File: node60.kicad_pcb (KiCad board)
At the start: 2 copper layers, 0 parts

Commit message: DEC-020: flipped 2.6 mm board, enclosure connector placement, 3D mockup
The board mounts component side down under the lid and is 2.6 mm thick,
so the SurLok Plus receptacles in the lid reach the REDCUBE 74660016R
terminals through the board (user's decisions, 2026-10-30).

- PCB: J901-J912 placed and locked, 250 x 160 mm provisional outline,
  2.6 mm thickness. Outputs on a 40 mm pitch; KiCad view mirrored
  against the outside view (scripts/place_connectors.py).
- Lid terminals on a symmetric grid: battery +-48 mm, return +-75 mm.
  scripts/check_surlok_clearance.py checks all 81 west/north/east plug
  combinations and keeps east/west plugs inside the walls.
- Architecture site: DEC-020, harness page section, Rev B entry, and the
  3D enclosure mockup served at /mockups/ (wrapped by the docs build).

Open: AT13/ATM13 pin tails protrude only 0.1-0.5 mm on 2.6 mm. CI now
runs DRC with schematic parity, which fails until layout is complete.

Co-Authored-By: Claude Opus 5.5 <noreply@anthropic.com>
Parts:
- added J901: 74660016R, DropOut_TerminalBlock_Wuerth:Wuerth_REDCUBE-SMT_WP-SMRT_74660016, F.Cu at (107.0, 125.0)
- added J902: 74660016R, DropOut_TerminalBlock_Wuerth:Wuerth_REDCUBE-SMT_WP-SMRT_74660016, F.Cu at (80.0, 65.0)
- added J903: ATM13-2P-BM04, DropOut_Connector_Amphenol:Amphenol_ATM13-2P-BMxx_1x02_P4.20mm_Horizontal, F.Cu at (46.0, 91.9)
- added J904: AT13-2P-BM04, DropOut_Connector_Amphenol:Amphenol_AT13-2P-BMxx_1x02_P5.40mm_Horizontal, F.Cu at (252.3, 175.0)
- added J905: AT13-2P-BM04, DropOut_Connector_Amphenol:Amphenol_AT13-2P-BMxx_1x02_P5.40mm_Horizontal, F.Cu at (212.3, 175.0)
- added J906: AT13-2P-BM04, DropOut_Connector_Amphenol:Amphenol_AT13-2P-BMxx_1x02_P5.40mm_Horizontal, F.Cu at (172.3, 175.0)
- added J907: AT13-2P-BM04, DropOut_Connector_Amphenol:Amphenol_AT13-2P-BMxx_1x02_P5.40mm_Horizontal, F.Cu at (132.3, 175.0)
- added J908: AT13-2P-BM04, DropOut_Connector_Amphenol:Amphenol_AT13-2P-BMxx_1x02_P5.40mm_Horizontal, F.Cu at (92.3, 175.0)
- added J909: AT13-2P-BM04, DropOut_Connector_Amphenol:Amphenol_AT13-2P-BMxx_1x02_P5.40mm_Horizontal, F.Cu at (52.3, 175.0)
- added J910: 74660016R, DropOut_TerminalBlock_Wuerth:Wuerth_REDCUBE-SMT_WP-SMRT_74660016, F.Cu at (203.0, 125.0)
- added J911: 74660016R, DropOut_TerminalBlock_Wuerth:Wuerth_REDCUBE-SMT_WP-SMRT_74660016, F.Cu at (230.0, 65.0)
- added J912: ATM13-2P-BM04, DropOut_Connector_Amphenol:Amphenol_ATM13-2P-BMxx_1x02_P4.20mm_Horizontal, F.Cu at (264.0, 96.1)
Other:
- board outline added: 250 x 160 mm

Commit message: DEC-021: board component side up, busbars, raised-T lid, T1S on north wall
The user changed the mechanical design on 2026-10-30 and accepted it after
reviewing the 3D mockup and the drawing. Supersedes DEC-020.

- PCB: component side up again (KiCad view = view from above). REDCUBE
  74660016R on B.Cu; J903/J912 in the middle of the north edge, 45 mm apart;
  lid terminals at +-70 mm, one battery/return pair each side. Busbar
  outlines on User.Drawings.
- Busbars: 1/8" x 1" C110 copper flat bar (25 x 3 mm metric), cut and drilled
  in house: 165.4 mm long, 2 x 6.5 mm holes 140 mm apart. The thinnest stock
  bar that carries the current, so most of the SurLok stud reaches the
  REDCUBE thread (stud length still to be confirmed with Amphenol).
- Lid: low sections where the receptacles sit on the busbars, and a raised T
  (crossbar over the outputs, stem over the T1S pair), derived from the
  header bodies.
- Plugs point outward or north: check_surlok_clearance.py checks all 16
  combinations against plugs, flanges, the T and the board edge.
- Enclosure drawing on engine 1.1 (stepped tops, staggered labels); the 3D
  mockup now reads the same enclosure.json, filled in by the docs build.

Co-Authored-By: Claude Opus 5.5 <noreply@anthropic.com>
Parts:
- J901, J902, J910, J911: moved to B.Cu
- moved J904 200.0 mm to (52.3, 175.0)
- moved J909 200.0 mm to (252.3, 175.0)
- moved J902 145.3 mm to (225.0, 75.0)
- moved J911 145.3 mm to (85.0, 75.0)
- moved J903 141.3 mm to (179.6, 46.0), turned to 180 degrees
- moved J912 138.8 mm to (134.6, 46.0), turned to 180 degrees
- moved J905 120.0 mm to (92.3, 175.0)
- moved J908 120.0 mm to (212.3, 175.0)
- moved J901 119.7 mm to (225.0, 145.0)
- moved J910 119.7 mm to (85.0, 145.0)
- moved J906 40.0 mm to (132.3, 175.0)
- moved J907 40.0 mm to (172.3, 175.0)
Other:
- board text added: "GND busbar 25.4 x 3.175 Cu (1/8 x 1 in C110), on top: no parts under it"
- board text added: "VBAT_IN busbar 25.4 x 3.175 Cu (1/8 x 1 in C110), on top: no parts under it"

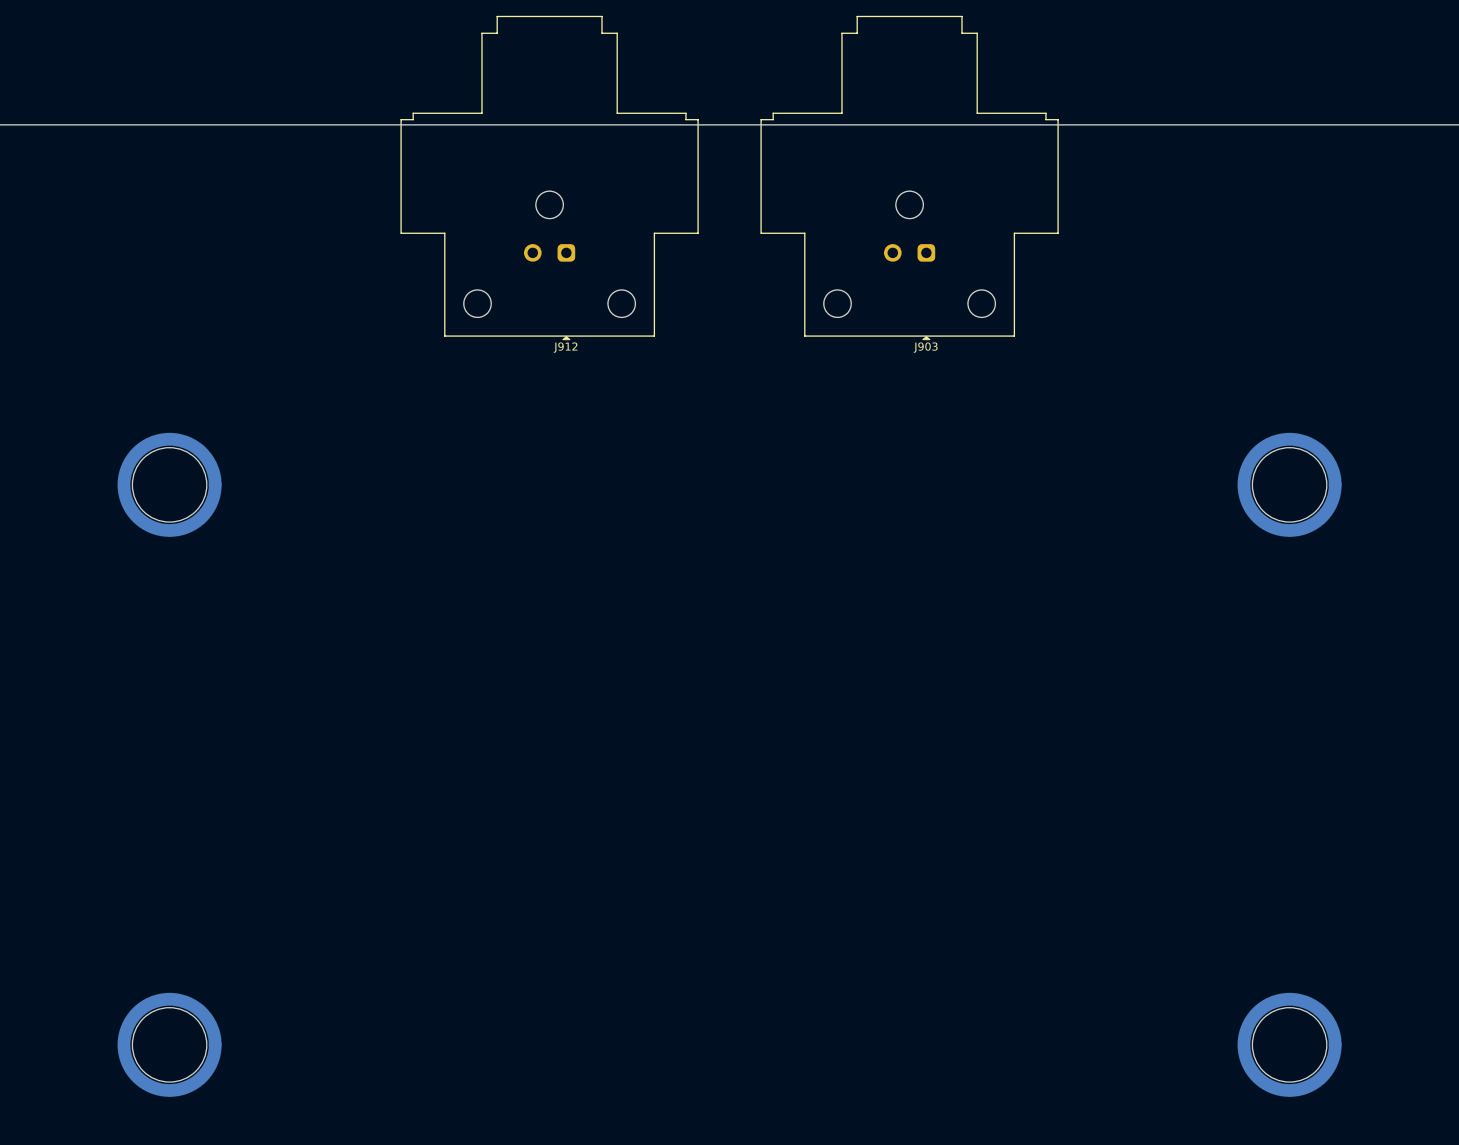
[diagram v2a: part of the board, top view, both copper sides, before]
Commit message: Version 2: staggered receptacles, T1S 41 mm apart; cable vs receptacles
The plug check now runs each plug's cable against the other
receptacles and plugs, not only the raised sections. It found that in
versions 2 and 4 a battery plug pointing north laid its cable over the
return receptacle behind it.

Versions 2 and 4: battery receptacles 57.5 mm and return 78.7 mm from
the centre line (were 70), so a north cable passes beside the return
receptacle. To make room beside the T stem, J903/J912 move from 45 to
41 mm apart (user; 41.98 mm is the most that works). Versions 6-8 keep
45 mm. node60.kicad_pcb re-placed (version 2); DRC with schematic
parity is clean. DEC-021 records the change.

Version 1 (superseded) now fails the cable check: inward plugs cross
the other receptacle. It is left as DEC-020's record.

Co-Authored-By: Claude Opus 5.5 <noreply@anthropic.com>
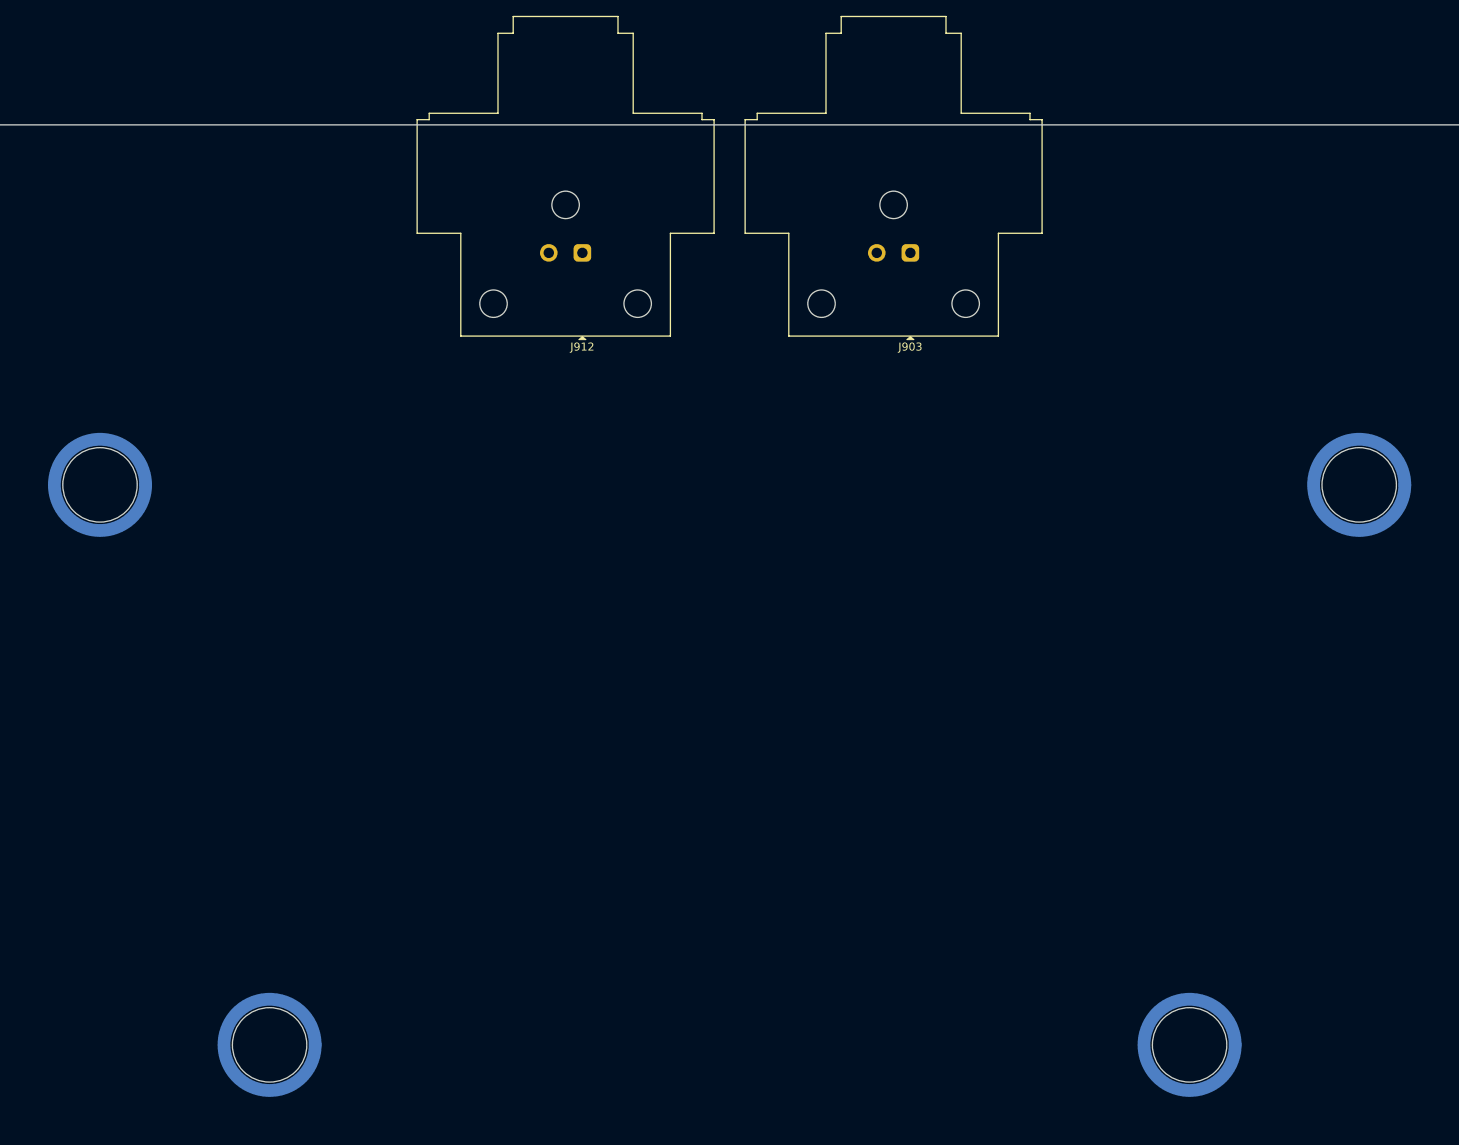
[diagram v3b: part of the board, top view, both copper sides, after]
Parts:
- moved J901 12.5 mm to (212.5, 145.0)
- moved J910 12.5 mm to (97.5, 145.0)
- moved J911 8.70 mm to (76.3, 75.0)
- moved J902 8.70 mm to (233.7, 75.0)
- moved J903 2.00 mm to (177.6, 46.0)
- moved J912 2.00 mm to (136.6, 46.0)
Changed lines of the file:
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@@
 		(locked yes)
 		(layer "F.Cu")
-		(at 179.6 46 180)
+		(at 177.6 46 180)
 		(descr "Amphenol Sine BoardLock ATM13-2P-BMxx 2-pin right-angle PCB receptacle with flange (mates ATM06-2S), 4.20 mm pitch, 3x #4-20 screw bosses; PCB layout and body per drawing ATM13-2P-BMXX rev. A2, https://www.amphenol-sine.com/pdf/datasheet/ATM13-2P-BM04.pdf")
 		(tags "connector Amphenol Sine ATM ATM13 ATM13-2P ATM06-2S BoardLock horizontal right angle sealed automotive")
@@
 		(locked yes)
 		(layer "F.Cu")
-		(at 134.6 46 180)
+		(at 136.6 46 180)
 		(descr "Amphenol Sine BoardLock ATM13-2P-BMxx 2-pin right-angle PCB receptacle with flange (mates ATM06-2S), 4.20 mm pitch, 3x #4-20 screw bosses; PCB layout and body per drawing ATM13-2P-BMXX rev. A2, https://www.amphenol-sine.com/pdf/datasheet/ATM13-2P-BM04.pdf")
 		(tags "connector Amphenol Sine ATM ATM13 ATM13-2P ATM06-2S BoardLock horizontal right angle sealed automotive")
@@
 		(locked yes)
 		(layer "B.Cu")
-		(at 85 145)
+		(at 97.5 145)
 		(descr "Würth REDCUBE SMT WP-SMRT, reverse with internal thread, M6, Ø12 flange, Ø9.3 non-plated hole for the Ø9.0 spigot, 85 A (data sheet 74660016 rev. 001.001 p. 1), https://www.we-online.com/components/products/datasheet/74660016.pdf")
 		(tags "REDCUBE SMT power terminal M6 internal thread reverse WP-SMRT 74660016 74660016R")
@@
 		(locked yes)
 		(layer "B.Cu")
-		(at 225 145)
+		(at 212.5 145)
 		(descr "Würth REDCUBE SMT WP-SMRT, reverse with internal thread, M6, Ø12 flange, Ø9.3 non-plated hole for the Ø9.0 spigot, 85 A (data sheet 74660016 rev. 001.001 p. 1), https://www.we-online.com/components/products/datasheet/74660016.pdf")
 		(tags "REDCUBE SMT power terminal M6 internal thread reverse WP-SMRT 74660016 74660016R")
@@
 		(locked yes)
 		(layer "B.Cu")
-		(at 85 75)
+		(at 76.3 75)
 		(descr "Würth REDCUBE SMT WP-SMRT, reverse with internal thread, M6, Ø12 flange, Ø9.3 non-plated hole for the Ø9.0 spigot, 85 A (data sheet 74660016 rev. 001.001 p. 1), https://www.we-online.com/components/products/datasheet/74660016.pdf")
 		(tags "REDCUBE SMT power terminal M6 internal thread reverse WP-SMRT 74660016 74660016R")
@@
 		(locked yes)
 		(layer "B.Cu")
-		(at 225 75)
+		(at 233.7 75)
 		(descr "Würth REDCUBE SMT WP-SMRT, reverse with internal thread, M6, Ø12 flange, Ø9.3 non-plated hole for the Ø9.0 spigot, 85 A (data sheet 74660016 rev. 001.001 p. 1), https://www.we-online.com/components/products/datasheet/74660016.pdf")
 		(tags "REDCUBE SMT power terminal M6 internal thread reverse WP-SMRT 74660016 74660016R")
@@
 	)
 	(gr_rect
-		(start 72.3 62.3)
-		(end 237.7 87.7)
+		(start 63.599999 62.3)
+		(end 246.399999 87.7)
 		(stroke
 			(width 0.15)
@@
 	)
 	(gr_rect
-		(start 72.3 132.3)
-		(end 237.7 157.7)
+		(start 84.8 132.3)
+		(end 225.2 157.7)
 		(stroke
 			(width 0.15)
